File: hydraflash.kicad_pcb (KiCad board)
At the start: 2 copper layers, 60 x 37 mm, 10 parts, among them J1 CONN_02X07, J2 CONN_02X10, J3 CONN_02X10, J4 CONN_01X06, P1 WRITE PROTECT, U1 Flash_NAND

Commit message: Routing improvements by bvernoux
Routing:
- net GND: track 70.0 -> 22.8 mm, vias 0 -> 6
- net +3V3: track 71.6 -> 106.1 mm
- net /PB1: track 29.4 -> 33.2 mm
- net Net-(P1-Pad2): track 19.8 -> 21.5 mm
- net /PB3: track 34.9 -> 33.8 mm
- net /PB2_BOOT1: track 31.7 -> 32.3 mm
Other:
- net class VCC added: clearance 0.1524, trace_width 0.3048, via_dia 0.6858, via_drill 0.3302

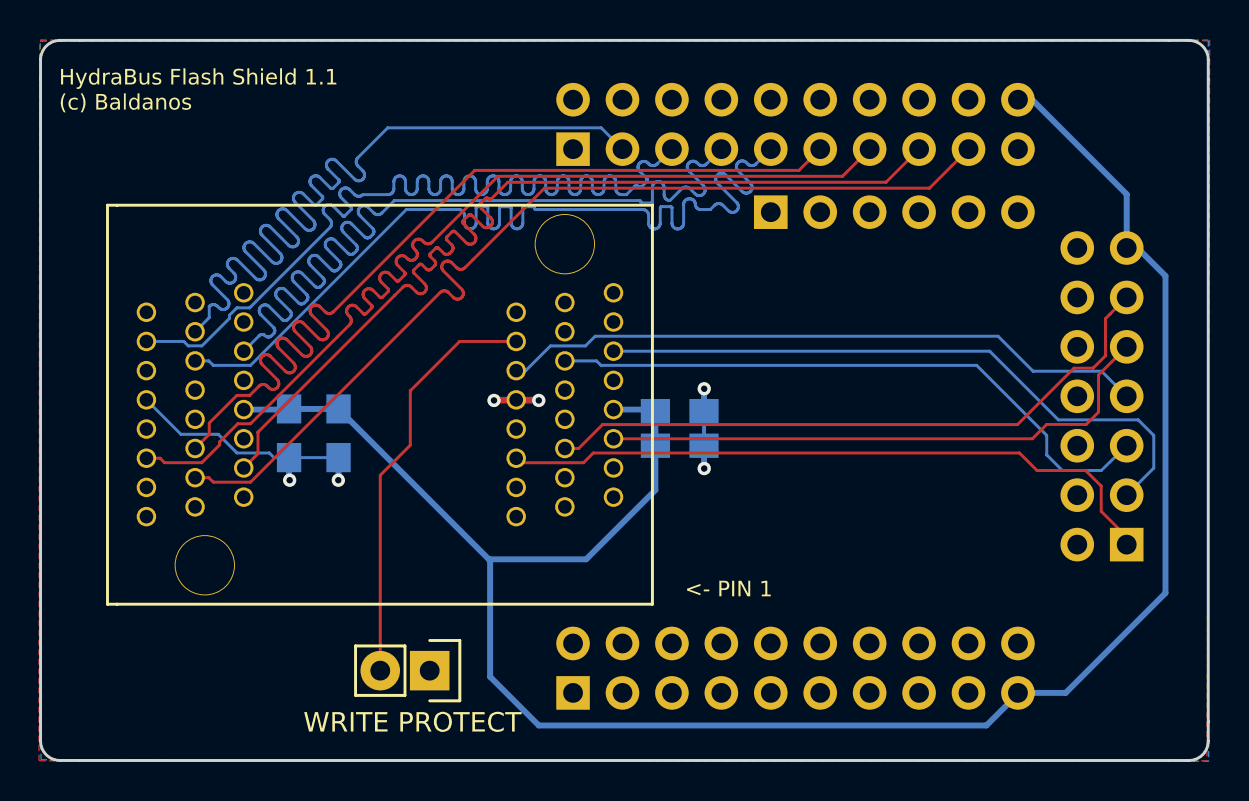
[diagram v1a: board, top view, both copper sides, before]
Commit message: Minor update(Capacitor values and 3V3 routing with bigger wire)
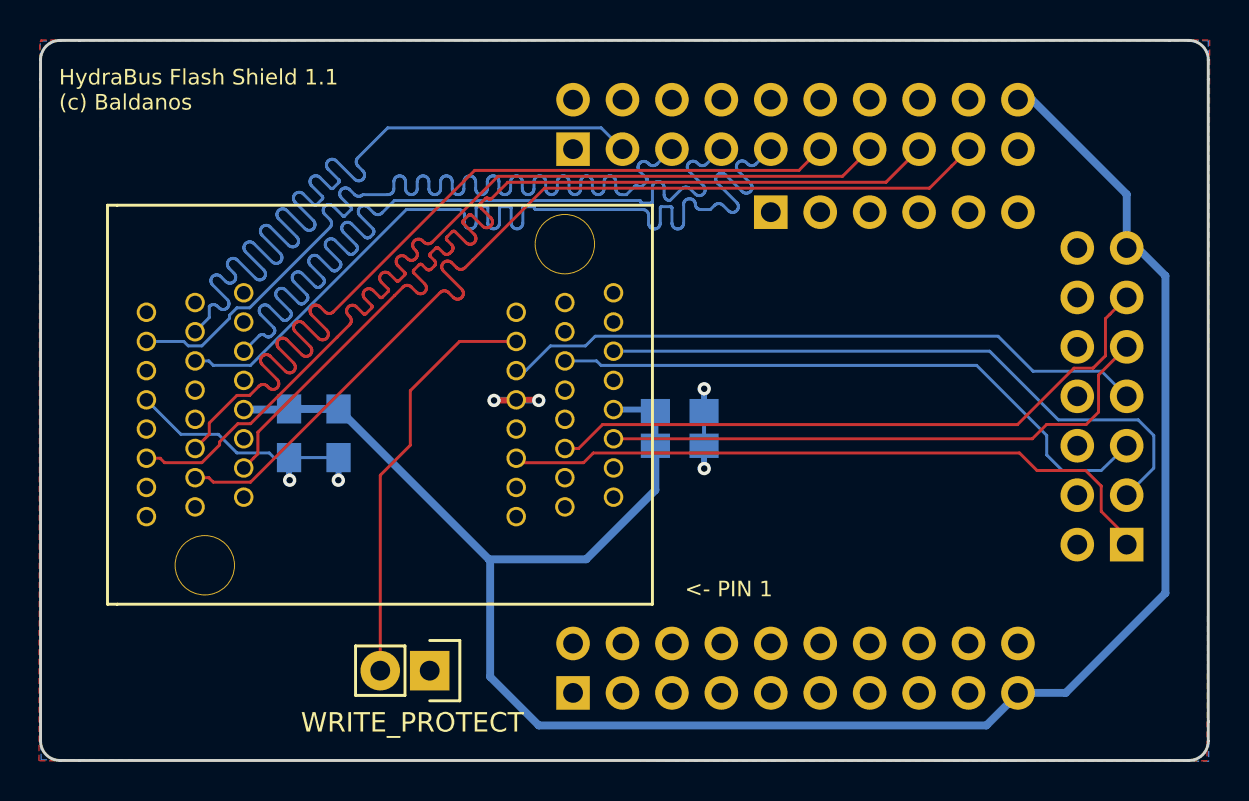
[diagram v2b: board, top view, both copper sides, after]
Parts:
- C1: value 1uF -> 100nF
- C2: value 100nF -> 1uF
- P1: value WRITE PROTECT -> WRITE_PROTECT
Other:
- net class VCC: trace_width 0.3048 -> 0.4064
